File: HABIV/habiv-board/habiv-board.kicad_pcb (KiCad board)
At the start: 4 copper layers, 100.3 x 120.9 mm, 126 parts, among them IC1 RTC_PCF8523T, J1 Micro_SD_Card_Det, J10 Conn_01x02_Female, J11 Conn_01x02_Female, J12 Conn_01x02_Female, J13 Conn_01x02_Female, J14 Conn_01x02_Female, J15 Conn_01x02_Female, J16 Conn_01x02_Female, J17 Conn_01x03_Male, J18 Conn_01x03_Male, J19 Conn_01x03_Male, J2 Conn_ARM_JTAG_SWD_20, J20 Conn_01x05_Male, J21 Conn_01x04_Male, J3 Conn_01x02_Male, J4 Conn_01x16_Male, J5 Conn_01x03_Male, J6 Conn_01x16_Male, J7 Conn_01x16_Male, J8 Conn_01x02_Female, J9 Conn_01x02_Male, Q1 32.768KHz, SW1 SW_DPST_x2, U1 STM32F401RET6, U2 MAX31855, U3 FGPMMOPA6H, U4 TPS564208, U5 TPS564208, U6 LSM9DS1TR, U7 MS560702BA03-00, Y1 32.768MHz

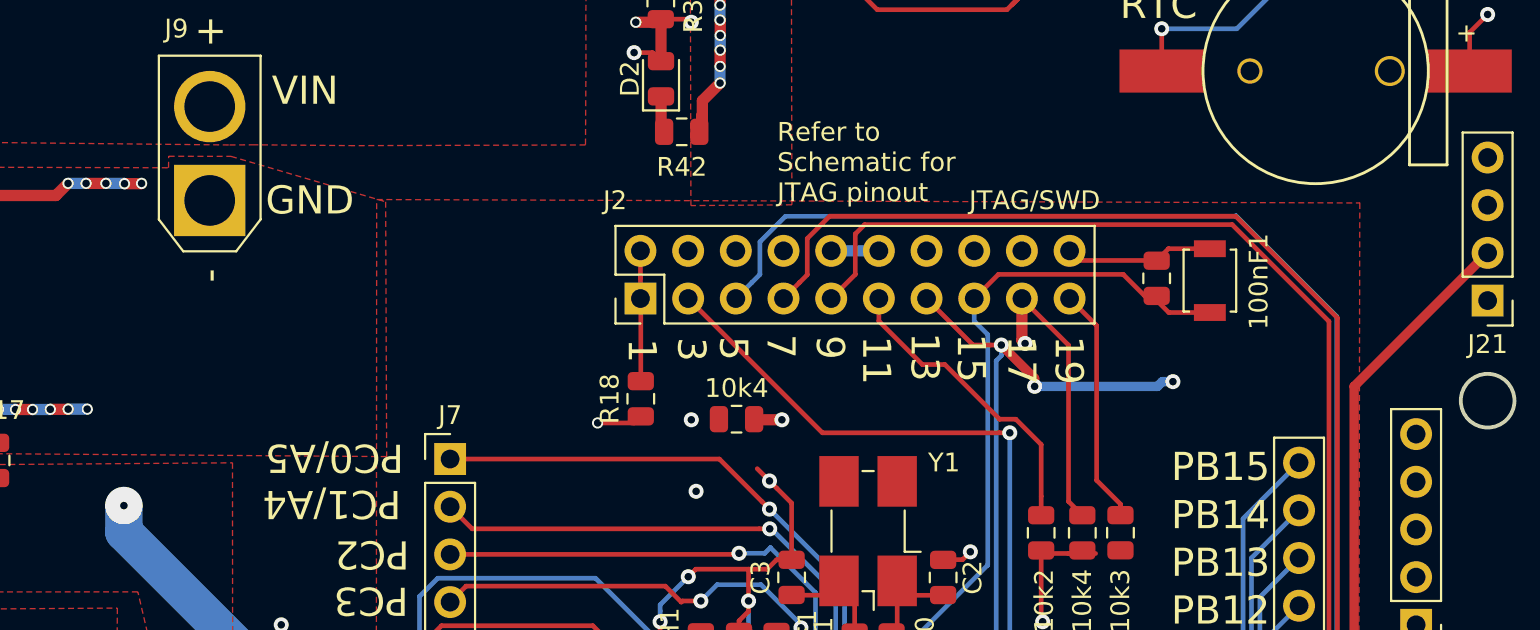
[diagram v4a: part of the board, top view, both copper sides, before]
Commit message: add final 5v conn
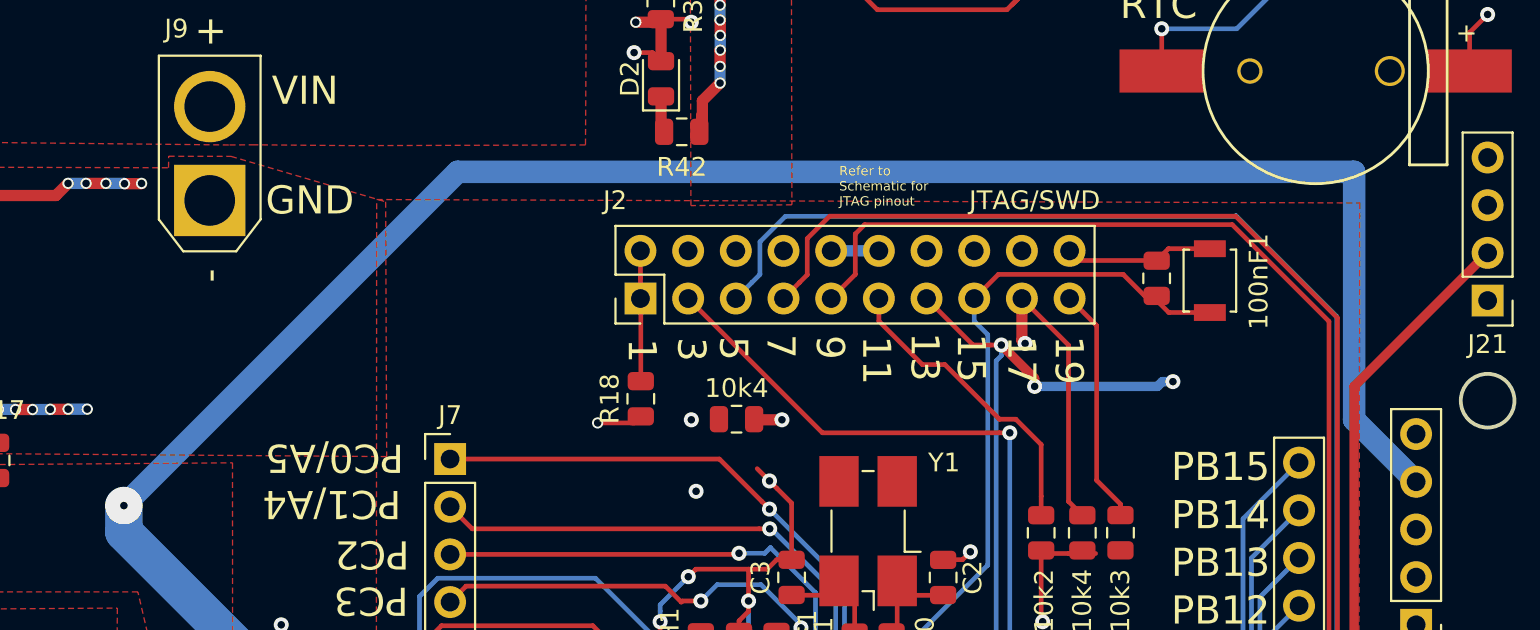
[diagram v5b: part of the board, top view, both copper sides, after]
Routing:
- net +5V: track 184.7 -> 275.5 mm
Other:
- net class Default: trace_width 0.5 -> 1.2
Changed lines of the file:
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@@
     (thickness 1.6)
     (drawings 83)
-    (tracks 2014)
+    (tracks 2018)
     (zones 0)
     (modules 126)
@@
   )
   (setup
-    (last_trace_width 0.5)
+    (last_trace_width 1.2)
     (trace_clearance 0.15)
     (zone_clearance 0)
@@
   (net_class Default "This is the default net class."
     (clearance 0.15)
-    (trace_width 0.5)
+    (trace_width 1.2)
     (via_dia 0.8)
     (via_drill 0.4)
@@
     (effects (font (size 1.5 1.5) (thickness 0.3)))
   )
-  (gr_text "Refer to\nSchematic for\nJTAG pinout" (at 139.7 58.674) (layer F.SilkS)
-    (effects (font (size 1 1) (thickness 0.25)) (justify left))
+  (gr_text "Refer to\nSchematic for\nJTAG pinout" (at 143.002 59.944) (layer F.SilkS)
+    (effects (font (size 0.5 0.5) (thickness 0.1)) (justify left))
   )
   (gr_text 19 (at 155.232527 69.218328 270) (layer F.SilkS)
@@
   (segment (start 142.688167 112.757168) (end 144.230999 114.3) (width 0.25) (layer F.Cu) (net 39) (status 20))
   (segment (start 144.230999 114.3) (end 148.689487 118.758488) (width 0.25) (layer F.Cu) (net 39) (status 20))
+  (segment (start 156.85059 97.398269) (end 156.85059 102.558269) (width 0.5) (layer In2.Cu) (net 39))
+  (segment (start 140.69432 81.241999) (end 156.85059 97.398269) (width 0.5) (layer In2.Cu) (net 39))
+  (segment (start 137.784316 81.241999) (end 140.69432 81.241999) (width 0.5) (layer In2.Cu) (net 39))
+  (segment (start 125.950769 69.408452) (end 137.784316 81.241999) (width 0.5) (layer In2.Cu) (net 39))
+  (segment (start 125.950769 43.988252) (end 125.950769 69.408452) (width 0.5) (layer In2.Cu) (net 39))
+  (segment (start 128.778 41.161021) (end 125.950769 43.988252) (width 0.5) (layer In2.Cu) (net 39))
+  (segment (start 128.778 16.002) (end 128.778 41.161021) (width 0.5) (layer In2.Cu) (net 39))
+  (segment (start 157.776768 103.484447) (end 157.776768 112.479232) (width 0.5) (layer In2.Cu) (net 39))
+  (segment (start 156.85059 102.558269) (end 157.776768 103.484447) (width 0.5) (layer In2.Cu) (net 39))
+  (via (at 155.448 114.046) (size 0.8) (drill 0.4) (layers F.Cu B.Cu) (net 39))
+  (segment (start 153.401975 114.046) (end 148.689487 118.758488) (width 0.5) (layer B.Cu) (net 39))
+  (segment (start 157.014768 112.479232) (end 155.448 114.046) (width 0.5) (layer In2.Cu) (net 39))
+  (segment (start 157.776768 112.479232) (end 157.014768 112.479232) (width 0.5) (layer In2.Cu) (net 39))
+  (segment (start 153.401975 114.046) (end 155.448 114.046) (width 0.5) (layer B.Cu) (net 39))
   (segment (start 143.188167 101.794548) (end 143.188167 110.717168) (width 0.25) (layer F.Cu) (net 40) (status 10))
   (segment (start 143.188167 110.717168) (end 151.229487 118.758488) (width 0.25) (layer F.Cu) (net 40) (status 20))
@@
   (segment (start 143.688167 101.794548) (end 143.688167 110.09779) (width 0.25) (layer F.Cu) (net 41) (status 10))
   (segment (start 143.688167 110.09779) (end 149.642085 116.051708) (width 0.25) (layer F.Cu) (net 41))
-  (segment (start 156.85059 97.398269) (end 156.85059 102.558269) (width 0.5) (layer In2.Cu) (net 39))
-  (segment (start 140.69432 81.241999) (end 156.85059 97.398269) (width 0.5) (layer In2.Cu) (net 39))
-  (segment (start 137.784316 81.241999) (end 140.69432 81.241999) (width 0.5) (layer In2.Cu) (net 39))
-  (segment (start 125.950769 69.408452) (end 137.784316 81.241999) (width 0.5) (layer In2.Cu) (net 39))
-  (segment (start 125.950769 43.988252) (end 125.950769 69.408452) (width 0.5) (layer In2.Cu) (net 39))
-  (segment (start 128.778 41.161021) (end 125.950769 43.988252) (width 0.5) (layer In2.Cu) (net 39))
-  (segment (start 128.778 16.002) (end 128.778 41.161021) (width 0.5) (layer In2.Cu) (net 39))
-  (segment (start 157.776768 103.484447) (end 157.776768 112.479232) (width 0.5) (layer In2.Cu) (net 39))
-  (segment (start 156.85059 102.558269) (end 157.776768 103.484447) (width 0.5) (layer In2.Cu) (net 39))
-  (via (at 155.448 114.046) (size 0.8) (drill 0.4) (layers F.Cu B.Cu) (net 39))
-  (segment (start 153.401975 114.046) (end 148.689487 118.758488) (width 0.5) (layer B.Cu) (net 39))
-  (segment (start 157.014768 112.479232) (end 155.448 114.046) (width 0.5) (layer In2.Cu) (net 39))
-  (segment (start 157.776768 112.479232) (end 157.014768 112.479232) (width 0.5) (layer In2.Cu) (net 39))
-  (segment (start 153.401975 114.046) (end 155.448 114.046) (width 0.5) (layer B.Cu) (net 39))
   (segment (start 164.296768 92.512449) (end 160.543217 96.266) (width 0.5) (layer In1.Cu) (net 41))
   (segment (start 169.400738 85.107262) (end 169.400738 87.324239) (width 0.5) (layer In1.Cu) (net 41))
@@
   (segment (start 126.238 22.745123) (end 107.804002 41.179121) (width 2) (layer B.Cu) (net 80))
   (segment (start 126.238 16.002) (end 126.238 22.745123) (width 2) (layer B.Cu) (net 80))
+  (segment (start 104.902 76.962) (end 122.682 59.182) (width 1.2) (layer B.Cu) (net 80))
+  (segment (start 122.682 59.182) (end 170.434 59.182) (width 1.2) (layer B.Cu) (net 80))
+  (segment (start 170.434 72.39) (end 173.736 75.692) (width 1.2) (layer B.Cu) (net 80))
+  (segment (start 170.434 59.182) (end 170.434 72.39) (width 1.2) (layer B.Cu) (net 80))
   (segment (start 133.51639 57.050289) (end 133.51639 55.328349) (width 0.6) (layer F.Cu) (net 81) (status 30))
   (segment (start 133.51639 55.328349) (end 133.51385 55.325809) (width 0.6) (layer F.Cu) (net 81) (status 30))

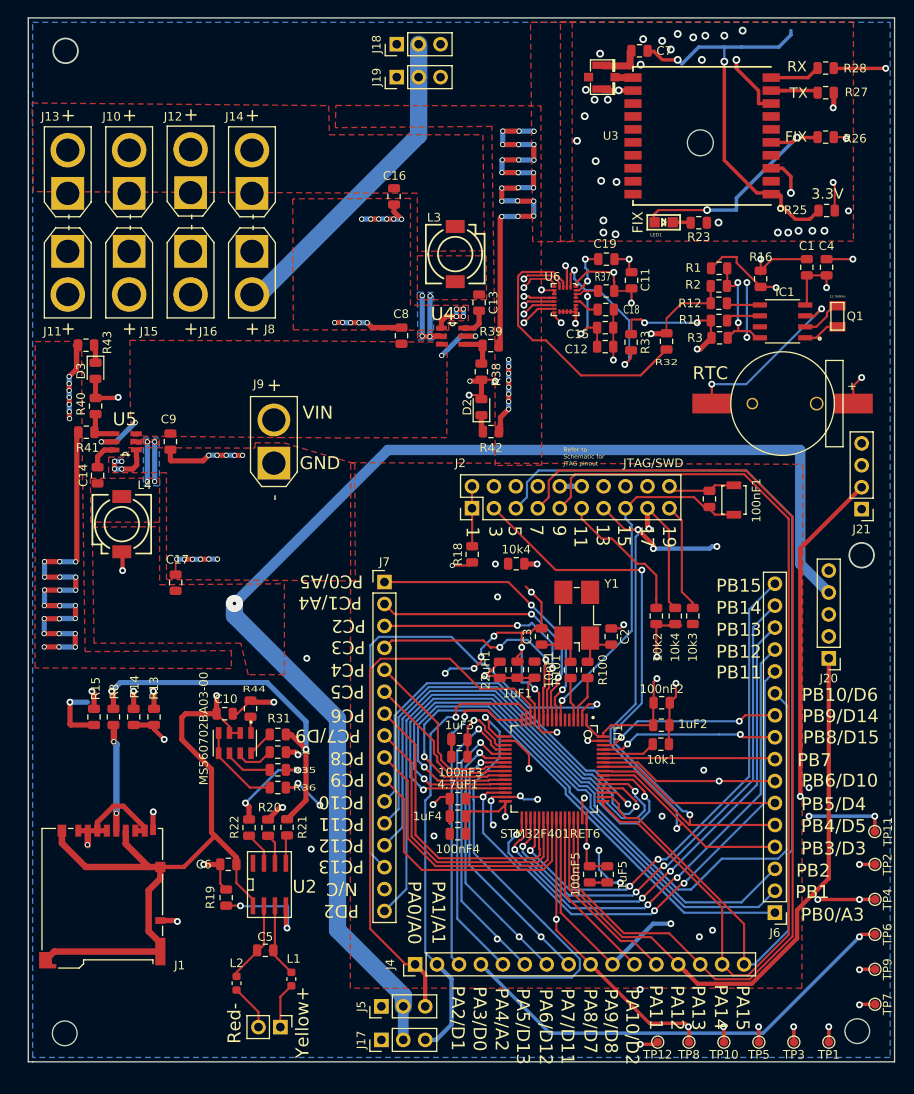
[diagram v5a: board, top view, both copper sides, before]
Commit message: add noise reducing caps and fix unconnected in1 plane
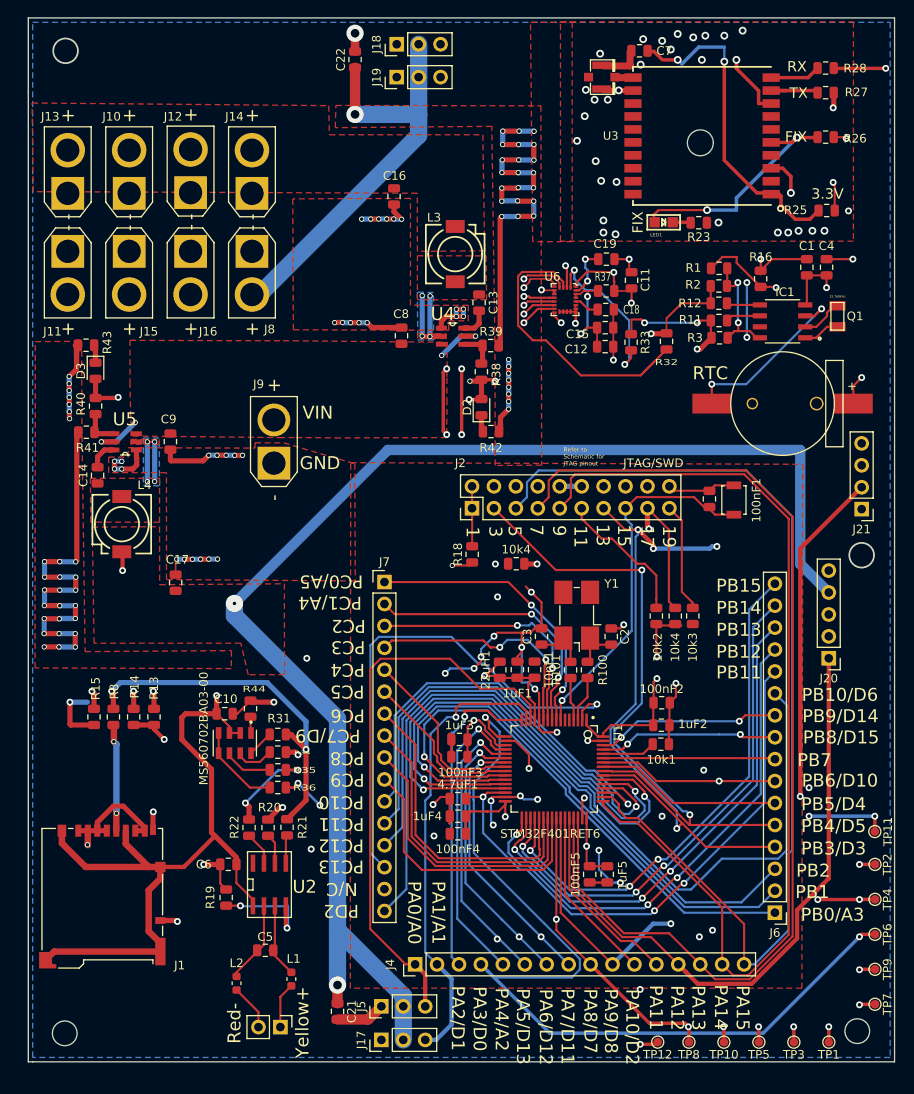
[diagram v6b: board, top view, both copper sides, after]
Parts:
- added C21: 10u, Capacitor_SMD:C_0805_2012Metric, F.Cu at (116.8, 124.2)
- added C22: 10u, Capacitor_SMD:C_0805_2012Metric, F.Cu at (118.9, 14.0)
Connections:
- IC1 pad 7: Net-(IC1-Pad7) -> (no net)
- J7 pad 15: Net-(J7-Pad15) -> (no net)
- U1 pad 5: Net-(U1-Pad5) -> (no net)
- U1 pad 6: Net-(U1-Pad6) -> (no net)
- U3 pad P$13: Net-(U3-PadP$13) -> (no net)
- U3 pad P$14: Net-(U3-PadP$14) -> (no net)
- U3 pad P$15: Net-(U3-PadP$15) -> (no net)
- U3 pad P$16: Net-(U3-PadP$16) -> (no net)
- U3 pad P$17: Net-(U3-PadP$17) -> (no net)
- U3 pad P$18: Net-(U3-PadP$18) -> (no net)
- U3 pad P$2: Net-(U3-PadP$2) -> (no net)
- U3 pad P$20: Net-(U3-PadP$20) -> (no net)
- U3 pad P$4: Net-(U3-PadP$4) -> (no net)
- U3 pad P$6: Net-(U3-PadP$6) -> (no net)
- U3 pad P$7: Net-(U3-PadP$7) -> (no net)
- Y1 pad 2: Net-(Y1-Pad2) -> (no net)
- Y1 pad 3: Net-(Y1-Pad3) -> (no net)
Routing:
- net +5V: track 275.5 -> 296.7 mm, vias 3 -> 5
- net Net-(C7-Pad1): track 47.1 -> 38.3 mm
- net GND: track 416.5 -> 424.3 mm, vias 146 -> 147
- net PC3: track 81.7 -> 82.1 mm, vias 3 -> 5
- net PC4: vias 1 -> 3
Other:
- net class Default: trace_width 1.2 -> 0.4

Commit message: update silkscreen text
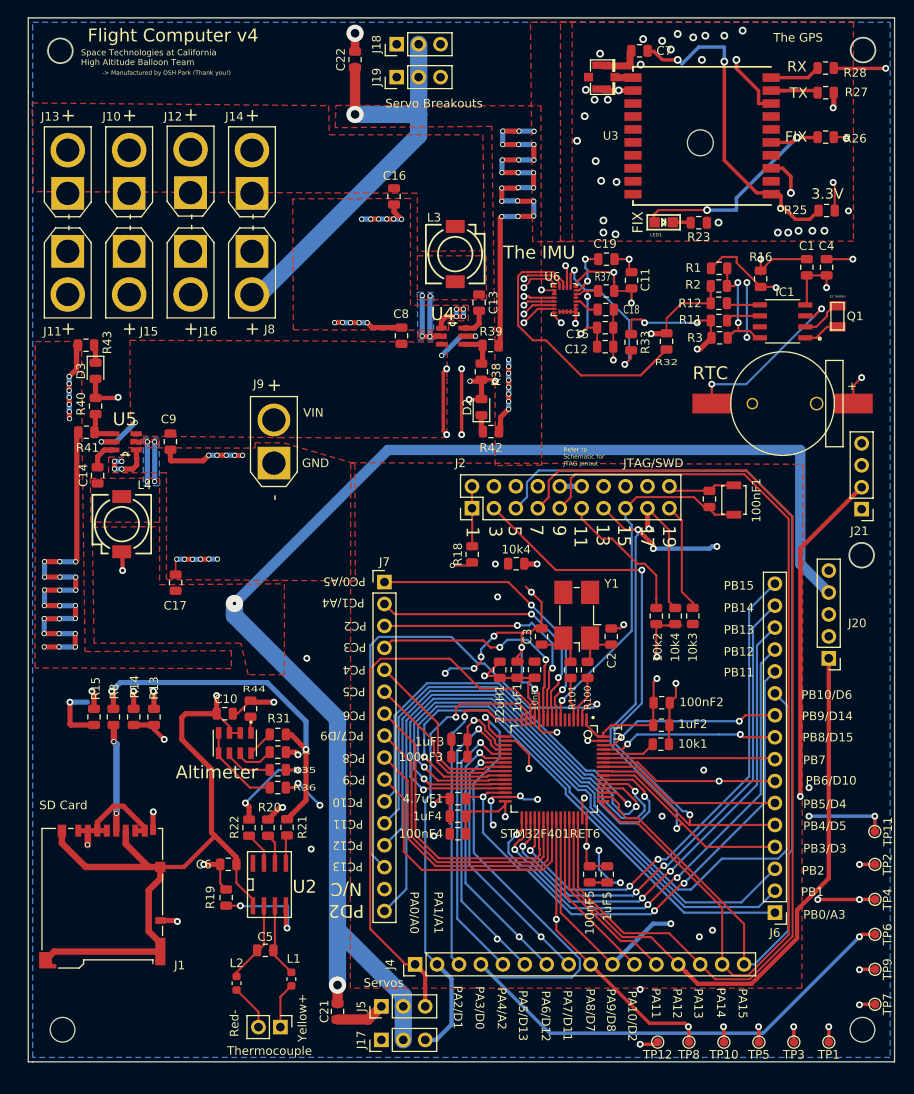
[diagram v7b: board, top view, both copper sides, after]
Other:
- outline, holes or cut-outs redrawn
- board text added: "-> Manufactured by OSH Park (Thank you!)"
- board text added: "Altimeter"
- board text added: "Flight Computer v4"
- board text added: "SD Card"
- board text added: "Servo Breakouts"
- board text added: "Servos"
- board text added: "Space Technologies at California High Altitude Balloon Team"
- board text added: "The GPS"
- board text added: "The IMU"
- board text added: "Thermocouple"

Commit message: gen stencil
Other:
- board text added: "HIGH ALTITUDE BRAIN"
- board text removed: "Flight Computer v4"
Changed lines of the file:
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@@
     )
   )
-  (gr_text "Flight Computer v4" (at 97.79 11.176) (layer F.SilkS)
-    (effects (font (size 1.5 1.5) (thickness 0.3)))
+  (gr_text "HIGH ALTITUDE BRAIN" (at 99.3 11.35) (layer F.SilkS)
+    (effects (font (size 1.5 1.5) (thickness 0.3) italic))
   )
   (gr_text "Space Technologies at California\nHigh Altitude Balloon Team" (at 87.122 13.716) (layer F.SilkS)
-    (effects (font (size 0.7 0.7) (thickness 0.1)) (justify left))
+    (effects (font (size 0.7 0.7) (thickness 0.1) italic) (justify left))
   )
   (gr_circle (center 177.706 12.86) (end 179.136 12.86) (layer Edge.Cuts) (width 0.2))
   (gr_text "-> Manufactured by OSH Park (Thank you!)" (at 97.028 15.494) (layer F.SilkS)
-    (effects (font (size 0.5 0.5) (thickness 0.1)))
+    (effects (font (size 0.5 0.5) (thickness 0.1) italic))
   )
   (gr_text Altimeter (at 102.87 96.52) (layer F.SilkS)
